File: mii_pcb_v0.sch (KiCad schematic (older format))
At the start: 8 parts, among them J1 CONN_02X05, J2 CONN_COAXIAL, J3 CONN_01X03, J4 CONN_01X03, J5 CONN_01X03, U1 WeMos_mini, U2 RFM69HW, U3 RFM69HCW

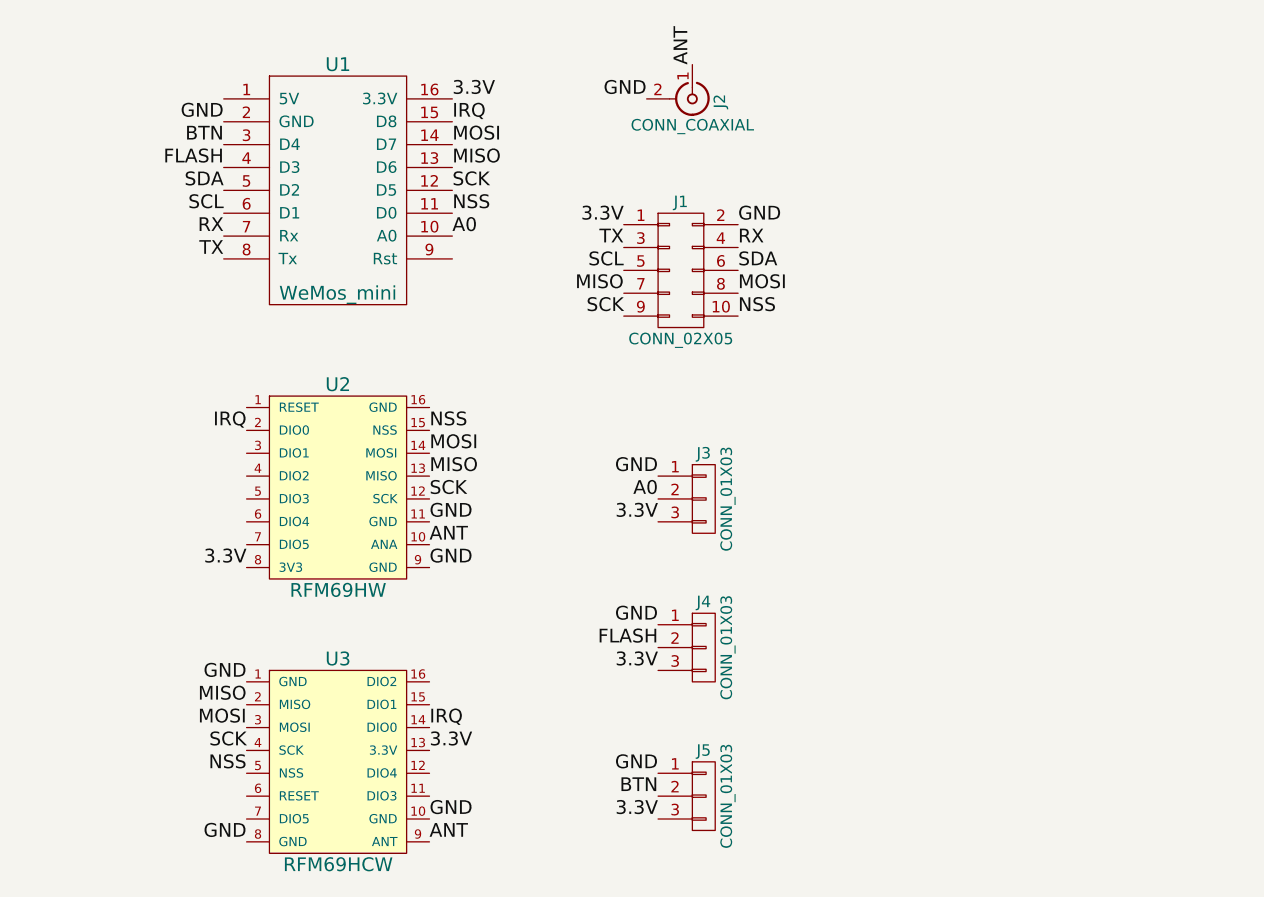
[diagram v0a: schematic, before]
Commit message: Add jumper for Deepsleep
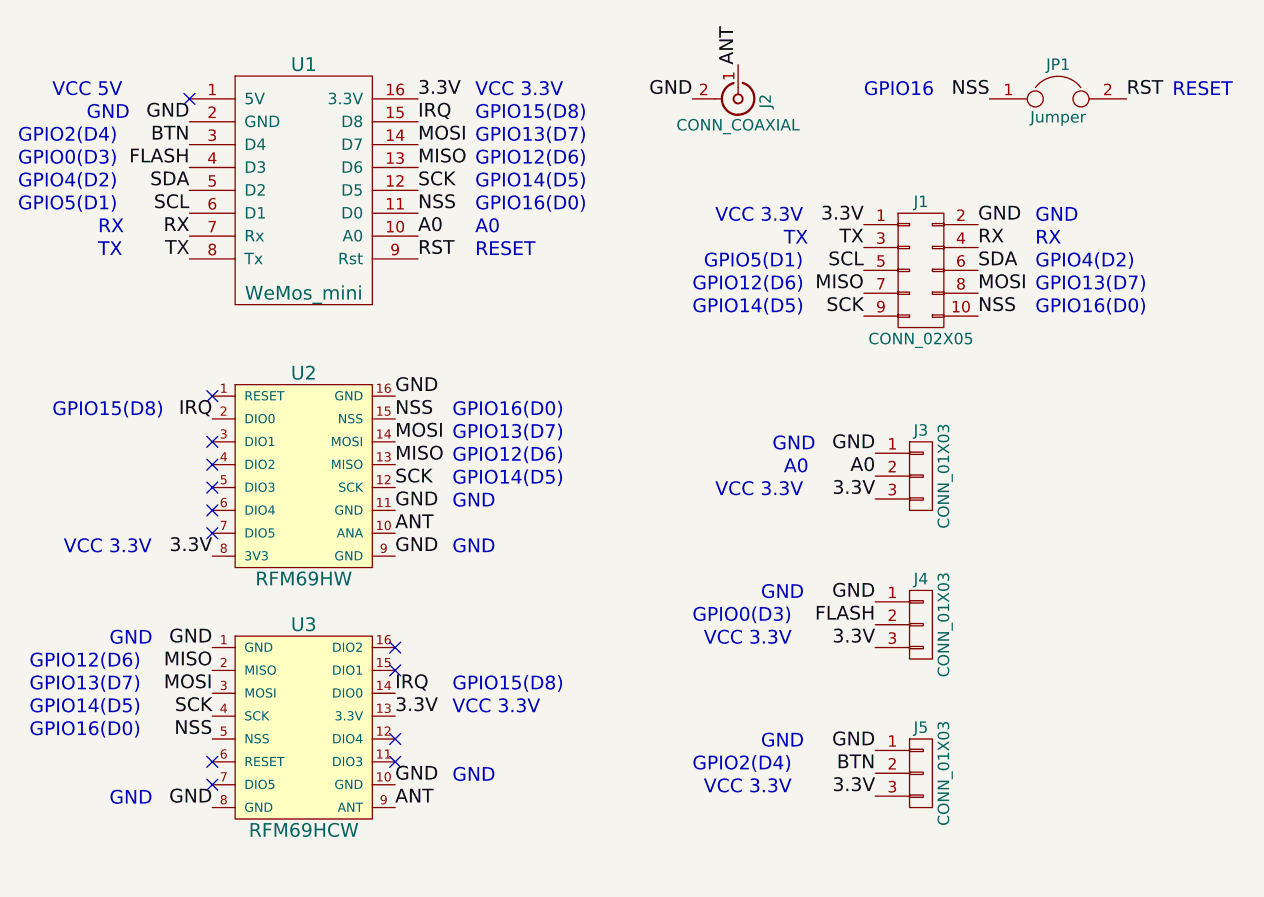
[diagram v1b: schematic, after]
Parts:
- added JP1: Jumper, Pin_Headers:Pin_Header_Straight_1x02_Pitch2.54mm, symbol Jumper
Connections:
- net GND: now also U2.16 (GND)
- net NSS: now also JP1.1
- net RST: now reaches U1.9 (Rst)
- net RST: now also JP1.2
- no-connect marks 0 -> 13
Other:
- note added: "A0"
- note added: "GND"
- note added: "GPIO0(D3)"
- note added: "GPIO12(D6)"
- note added: "GPIO13(D7)"
- note added: "GPIO14(D5)"
- note added: "GPIO15(D8)"
- note added: "GPIO16"
- note added: "GPIO16(D0)"
- note added: "GPIO2(D4)"
- note added: "GPIO4(D2)"
- note added: "GPIO5(D1)"
- note added: "RESET"
- note added: "RX"
- note added: "TX"
- note added: "VCC 3.3V"
- note added: "VCC 5V"
- moved on the sheet: J1, J2, J3, J4, J5, U1, U2, U3
